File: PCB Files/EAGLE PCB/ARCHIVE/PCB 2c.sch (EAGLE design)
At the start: 13 parts

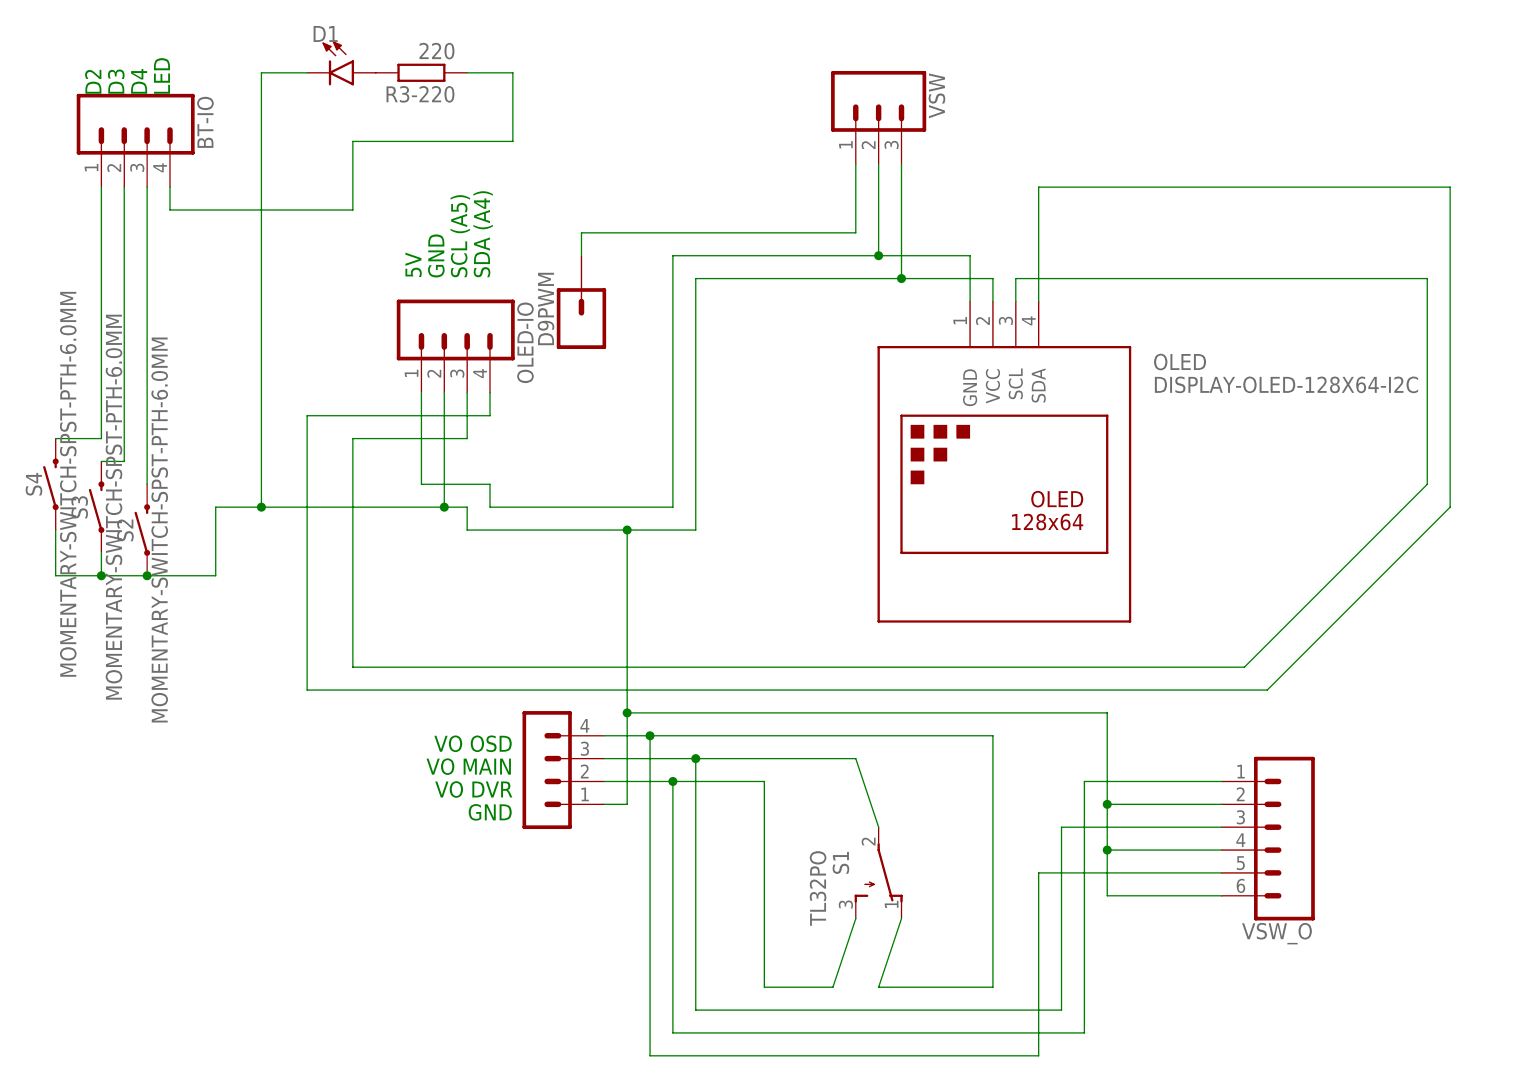
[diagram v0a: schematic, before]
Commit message: Updated PCBs
• Round edges
• Covered vias on PCB1
• OLED pin swap (VCC <> GND) on PCB2
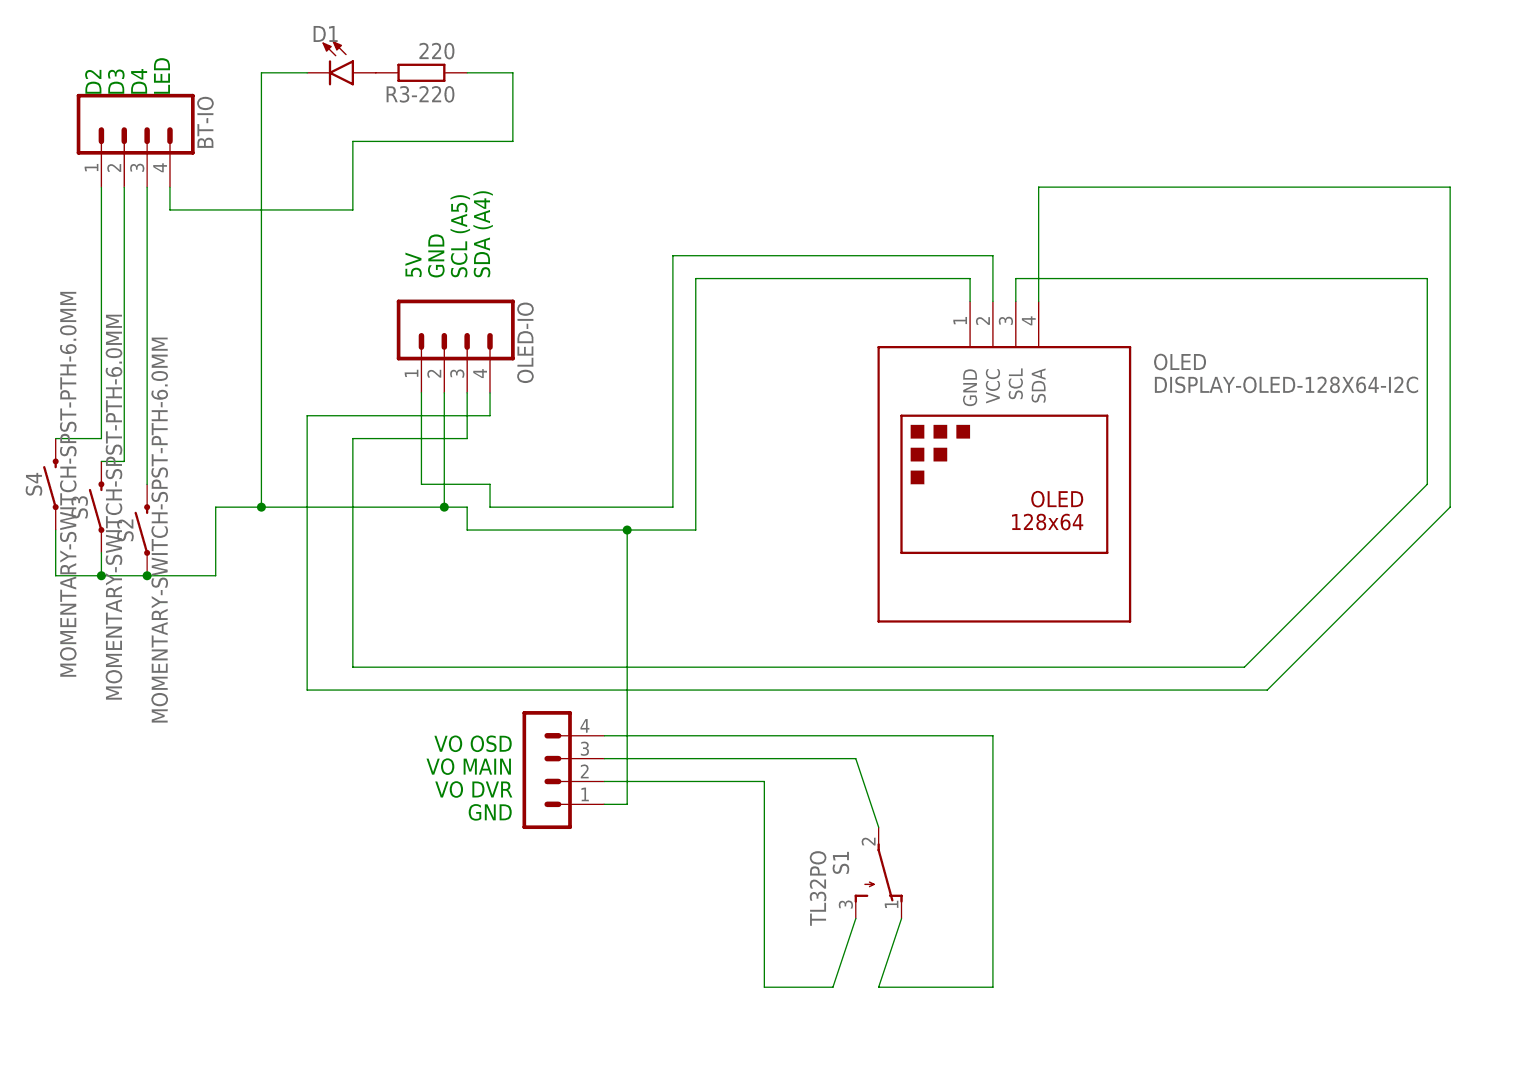
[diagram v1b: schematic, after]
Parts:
- removed D9PWM: (no value), SparkFun-Connectors:CONN_01
- removed VSW: (no value), SparkFun-Connectors:CONN_03
- removed VSW_O: (no value), SparkFun-Connectors:CONN_06SILK_FEMALE_PTH
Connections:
- removed net N$8: D9PWM.1, VSW.1
- net GND: now also OLED.GND; no longer OLED.VCC, VSW.3, VSW_O.2, VSW_O.4, VSW_O.6
- net N$10: no longer VSW_O.1
- net N$3: no longer VSW_O.3
- net N$4: now also OLED.VCC; no longer OLED.GND, VSW.2
- net VIDOUT: no longer VSW_O.5
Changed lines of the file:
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@@
 <part name="D1" library="SparkFun-LED" library_urn="urn:adsk.eagle:library:529" deviceset="LED" device="3MM" package3d_urn="urn:adsk.eagle:package:39361/1"/>
 <part name="R3-220" library="resistor" library_urn="urn:adsk.eagle:library:348" deviceset="R-EU_" device="R1206" package3d_urn="urn:adsk.eagle:package:26062/1" value="220"/>
-<part name="D9PWM" library="SparkFun-Connectors" library_urn="urn:adsk.eagle:library:513" deviceset="CONN_01" device="" package3d_urn="urn:adsk.eagle:package:38028/1"/>
-<part name="VSW" library="SparkFun-Connectors" library_urn="urn:adsk.eagle:library:513" deviceset="CONN_03" device="" package3d_urn="urn:adsk.eagle:package:38063/1"/>
-<part name="VSW_O" library="SparkFun-Connectors" library_urn="urn:adsk.eagle:library:513" deviceset="CONN_06" device="SILK_FEMALE_PTH" package3d_urn="urn:adsk.eagle:package:38009/1"/>
 </parts>
 <sheets>
@@
 <instance part="D1" gate="G$1" x="86.36" y="220.98" rot="R270"/>
 <instance part="R3-220" gate="G$1" x="93.98" y="220.98" rot="R180"/>
-<instance part="D9PWM" gate="G$1" x="111.76" y="193.04" rot="R90"/>
-<instance part="VSW" gate="J$1" x="144.78" y="218.44" rot="R270"/>
-<instance part="VSW_O" gate="G$1" x="187.96" y="137.16" rot="R180"/>
 </instances>
 <busses>
@@
 <segment>
 <pinref part="IO3" gate="1" pin="4"/>
-<wire x1="114.3" y1="147.32" x2="119.38" y2="147.32" width="0.1524" layer="91"/>
-<wire x1="119.38" y1="147.32" x2="157.48" y2="147.32" width="0.1524" layer="91"/>
+<wire x1="114.3" y1="147.32" x2="157.48" y2="147.32" width="0.1524" layer="91"/>
 <wire x1="157.48" y1="147.32" x2="157.48" y2="119.38" width="0.1524" layer="91"/>
 <wire x1="157.48" y1="119.38" x2="144.78" y2="119.38" width="0.1524" layer="91"/>
 <pinref part="S1" gate="BEF1" pin="O"/>
 <wire x1="144.78" y1="119.38" x2="147.32" y2="127" width="0.1524" layer="91"/>
-<pinref part="VSW_O" gate="G$1" pin="5"/>
-<wire x1="182.88" y1="132.08" x2="162.56" y2="132.08" width="0.1524" layer="91"/>
-<wire x1="162.56" y1="132.08" x2="162.56" y2="111.76" width="0.1524" layer="91"/>
-<wire x1="162.56" y1="111.76" x2="119.38" y2="111.76" width="0.1524" layer="91"/>
-<wire x1="119.38" y1="111.76" x2="119.38" y2="147.32" width="0.1524" layer="91"/>
-<junction x="119.38" y="147.32"/>
 </segment>
 </net>
@@
 <segment>
 <pinref part="IO3" gate="1" pin="3"/>
-<wire x1="114.3" y1="144.78" x2="124.46" y2="144.78" width="0.1524" layer="91"/>
+<wire x1="114.3" y1="144.78" x2="142.24" y2="144.78" width="0.1524" layer="91"/>
 <pinref part="S1" gate="BEF1" pin="P"/>
-<wire x1="124.46" y1="144.78" x2="142.24" y2="144.78" width="0.1524" layer="91"/>
 <wire x1="142.24" y1="144.78" x2="144.78" y2="137.16" width="0.1524" layer="91"/>
-<pinref part="VSW_O" gate="G$1" pin="3"/>
-<wire x1="182.88" y1="137.16" x2="165.1" y2="137.16" width="0.1524" layer="91"/>
-<wire x1="165.1" y1="137.16" x2="165.1" y2="116.84" width="0.1524" layer="91"/>
-<wire x1="165.1" y1="116.84" x2="124.46" y2="116.84" width="0.1524" layer="91"/>
-<wire x1="124.46" y1="116.84" x2="124.46" y2="144.78" width="0.1524" layer="91"/>
-<junction x="124.46" y="144.78"/>
 </segment>
 </net>
@@
 <wire x1="116.84" y1="170.18" x2="124.46" y2="170.18" width="0.1524" layer="91"/>
 <wire x1="124.46" y1="170.18" x2="124.46" y2="198.12" width="0.1524" layer="91"/>
-<wire x1="124.46" y1="198.12" x2="147.32" y2="198.12" width="0.1524" layer="91"/>
-<wire x1="147.32" y1="198.12" x2="157.48" y2="198.12" width="0.1524" layer="91"/>
+<wire x1="124.46" y1="198.12" x2="154.94" y2="198.12" width="0.1524" layer="91"/>
+<pinref part="OLED" gate="G$1" pin="GND"/>
+<wire x1="154.94" y1="198.12" x2="154.94" y2="195.58" width="0.1524" layer="91"/>
 <pinref part="IO3" gate="1" pin="1"/>
 <wire x1="99.06" y1="172.72" x2="96.52" y2="172.72" width="0.1524" layer="91"/>
@@
 <wire x1="76.2" y1="172.72" x2="71.12" y2="172.72" width="0.1524" layer="91"/>
 <wire x1="116.84" y1="139.7" x2="114.3" y2="139.7" width="0.1524" layer="91"/>
-<wire x1="116.84" y1="139.7" x2="116.84" y2="149.86" width="0.1524" layer="91"/>
+<wire x1="116.84" y1="139.7" x2="116.84" y2="170.18" width="0.1524" layer="91"/>
 <junction x="116.84" y="170.18"/>
-<wire x1="116.84" y1="149.86" x2="116.84" y2="170.18" width="0.1524" layer="91"/>
 <wire x1="71.12" y1="172.72" x2="71.12" y2="165.1" width="0.1524" layer="91"/>
 <pinref part="S2" gate="G$1" pin="1"/>
@@
 <wire x1="76.2" y1="220.98" x2="76.2" y2="172.72" width="0.1524" layer="91"/>
 <junction x="76.2" y="172.72"/>
-<pinref part="VSW" gate="J$1" pin="3"/>
-<wire x1="147.32" y1="210.82" x2="147.32" y2="198.12" width="0.1524" layer="91"/>
-<junction x="147.32" y="198.12"/>
-<junction x="116.84" y="149.86"/>
-<wire x1="170.18" y1="149.86" x2="116.84" y2="149.86" width="0.1524" layer="91"/>
-<wire x1="170.18" y1="149.86" x2="170.18" y2="139.7" width="0.1524" layer="91"/>
-<pinref part="VSW_O" gate="G$1" pin="6"/>
-<wire x1="170.18" y1="139.7" x2="170.18" y2="134.62" width="0.1524" layer="91"/>
-<wire x1="170.18" y1="134.62" x2="170.18" y2="129.54" width="0.1524" layer="91"/>
-<wire x1="170.18" y1="129.54" x2="182.88" y2="129.54" width="0.1524" layer="91"/>
-<pinref part="VSW_O" gate="G$1" pin="4"/>
-<wire x1="182.88" y1="134.62" x2="170.18" y2="134.62" width="0.1524" layer="91"/>
-<junction x="170.18" y="134.62"/>
-<pinref part="VSW_O" gate="G$1" pin="2"/>
-<wire x1="182.88" y1="139.7" x2="170.18" y2="139.7" width="0.1524" layer="91"/>
-<junction x="170.18" y="139.7"/>
-<pinref part="OLED" gate="G$1" pin="VCC"/>
-<wire x1="157.48" y1="195.58" x2="157.48" y2="198.12" width="0.1524" layer="91"/>
 </segment>
 </net>
 <net name="N$4" class="0">
 <segment>
-<wire x1="144.78" y1="200.66" x2="121.92" y2="200.66" width="0.1524" layer="91"/>
+<pinref part="OLED" gate="G$1" pin="VCC"/>
+<wire x1="157.48" y1="195.58" x2="157.48" y2="200.66" width="0.1524" layer="91"/>
+<wire x1="157.48" y1="200.66" x2="121.92" y2="200.66" width="0.1524" layer="91"/>
 <wire x1="121.92" y1="200.66" x2="121.92" y2="172.72" width="0.1524" layer="91"/>
 <wire x1="101.6" y1="172.72" x2="121.92" y2="172.72" width="0.1524" layer="91"/>
@@
 <pinref part="OLED-IO" gate="G$1" pin="1"/>
 <wire x1="93.98" y1="185.42" x2="93.98" y2="175.26" width="0.1524" layer="91"/>
-<pinref part="VSW" gate="J$1" pin="2"/>
-<wire x1="144.78" y1="210.82" x2="144.78" y2="200.66" width="0.1524" layer="91"/>
-<pinref part="OLED" gate="G$1" pin="GND"/>
-<wire x1="154.94" y1="195.58" x2="154.94" y2="200.66" width="0.1524" layer="91"/>
-<wire x1="154.94" y1="200.66" x2="144.78" y2="200.66" width="0.1524" layer="91"/>
-<junction x="144.78" y="200.66"/>
 </segment>
 </net>
@@
 <segment>
 <pinref part="IO3" gate="1" pin="2"/>
-<wire x1="114.3" y1="142.24" x2="121.92" y2="142.24" width="0.1524" layer="91"/>
-<wire x1="121.92" y1="142.24" x2="132.08" y2="142.24" width="0.1524" layer="91"/>
+<wire x1="114.3" y1="142.24" x2="132.08" y2="142.24" width="0.1524" layer="91"/>
 <wire x1="132.08" y1="142.24" x2="132.08" y2="119.38" width="0.1524" layer="91"/>
 <wire x1="132.08" y1="119.38" x2="139.7" y2="119.38" width="0.1524" layer="91"/>
 <pinref part="S1" gate="BEF1" pin="S"/>
 <wire x1="139.7" y1="119.38" x2="142.24" y2="127" width="0.1524" layer="91"/>
-<pinref part="VSW_O" gate="G$1" pin="1"/>
-<wire x1="182.88" y1="142.24" x2="167.64" y2="142.24" width="0.1524" layer="91"/>
-<wire x1="167.64" y1="142.24" x2="167.64" y2="114.3" width="0.1524" layer="91"/>
-<wire x1="167.64" y1="114.3" x2="121.92" y2="114.3" width="0.1524" layer="91"/>
-<wire x1="121.92" y1="114.3" x2="121.92" y2="142.24" width="0.1524" layer="91"/>
-<junction x="121.92" y="142.24"/>
 </segment>
 </net>
@@
 </segment>
 </net>
-<net name="N$8" class="0">
-<segment>
-<pinref part="VSW" gate="J$1" pin="1"/>
-<wire x1="142.24" y1="210.82" x2="142.24" y2="203.2" width="0.1524" layer="91"/>
-<wire x1="142.24" y1="203.2" x2="111.76" y2="203.2" width="0.1524" layer="91"/>
-<pinref part="D9PWM" gate="G$1" pin="1"/>
-<wire x1="111.76" y1="203.2" x2="111.76" y2="200.66" width="0.1524" layer="91"/>
-</segment>
-</net>
